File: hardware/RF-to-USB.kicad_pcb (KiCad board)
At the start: 4 copper layers, 48 x 21.5 mm, 6 parts, among them J1 USB_A, J2 Conn_Coaxial, U1 nRF24L01P, U2 STM32L432KBUx, U3 XC6206P332MR, U4 USBLC6-2SC6

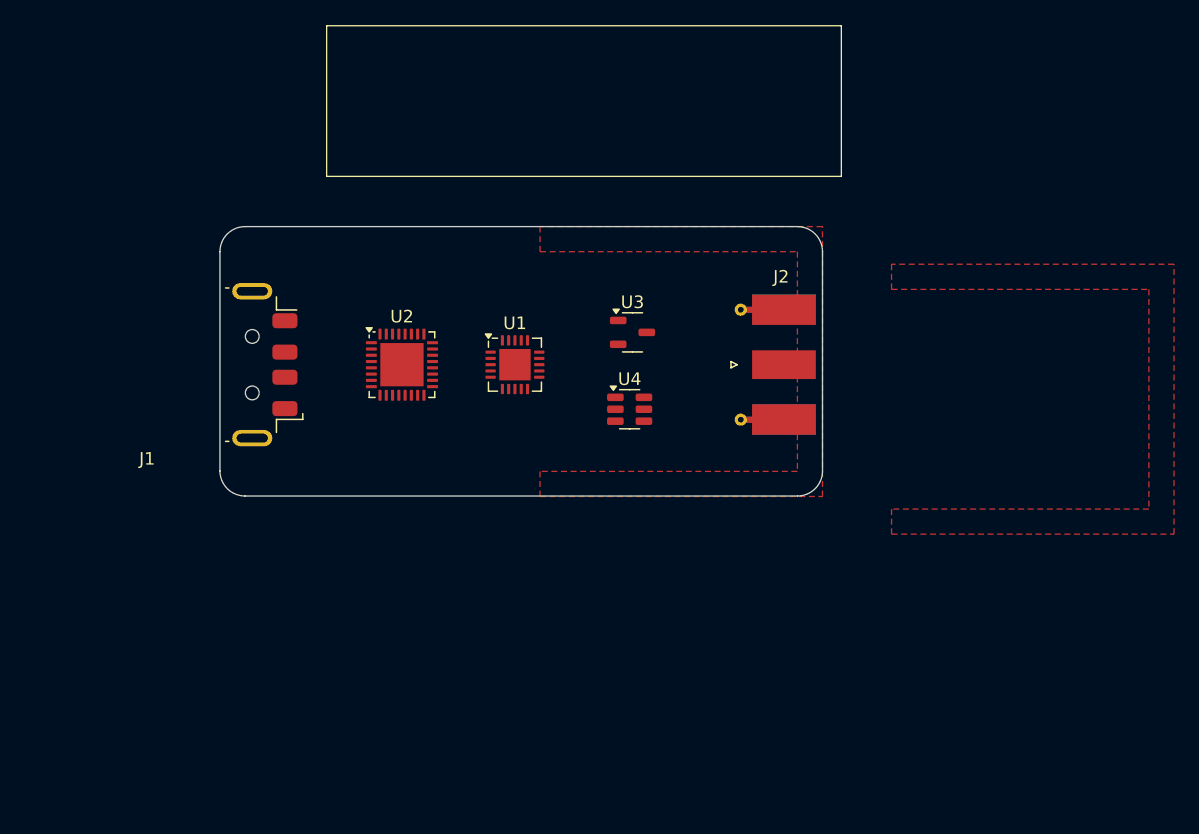
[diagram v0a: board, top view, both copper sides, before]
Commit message: NRF24 transceiver schematic
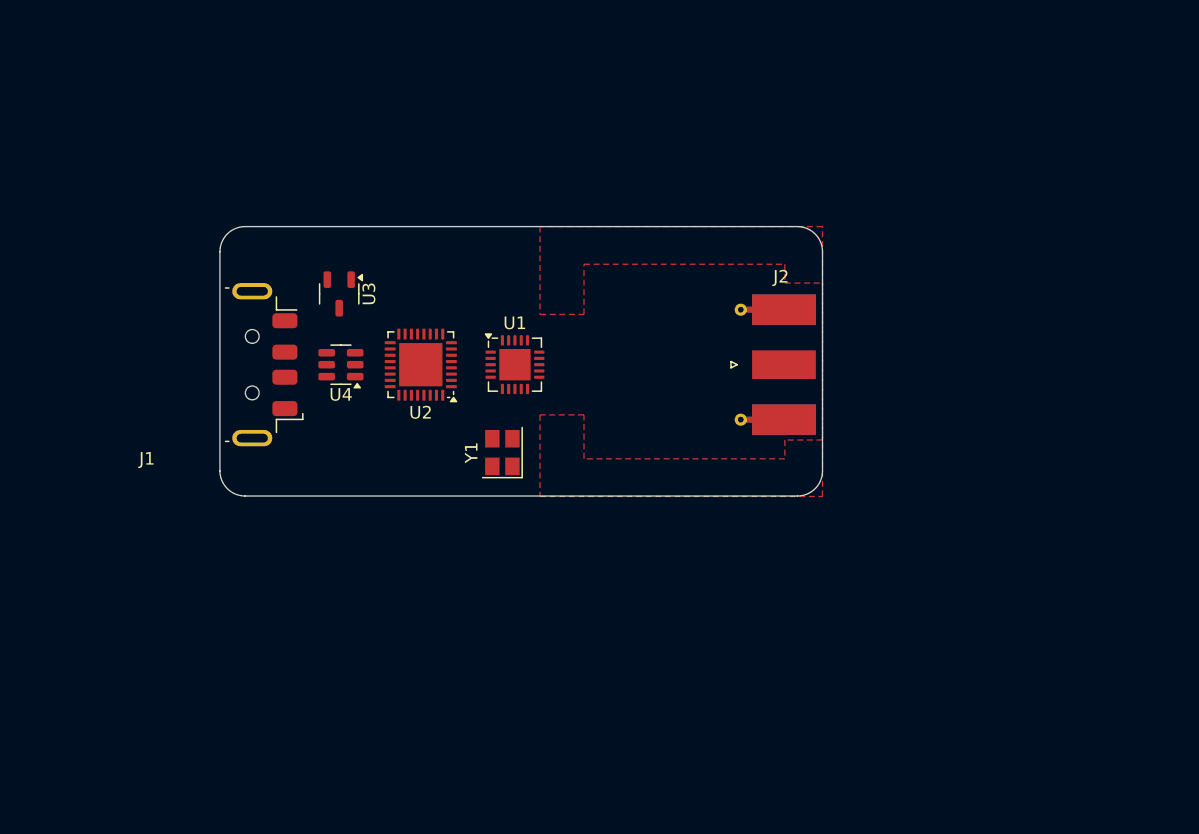
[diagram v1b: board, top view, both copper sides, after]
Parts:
- added Y1: 16MHz, Crystal:Crystal_SMD_SeikoEpson_TSX3225-4Pin_3.2x2.5mm, F.Cu at (98.0, 55.5)
- J2: value Conn_Coaxial -> SMA-F
- moved U3 23.6 mm to (85.0, 42.9), turned to -90 degrees
- moved U4 23.3 mm to (85.1, 48.5), turned to 180 degrees
- moved U2 1.50 mm to (91.5, 48.5), turned to 180 degrees
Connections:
- net Net-(J1-D+) renamed /USB_A_D+
- net Net-(J1-D-) renamed /USB_A_D-
- J2 pad 1: unconnected-(J2-In-Pad1) -> /NRF_ANT
- J2 pad 2: unconnected-(J2-Ext-Pad2) -> GND
- U1 pad 1: unconnected-(U1-CE-Pad1) -> NRF_CE
- U1 pad 10: unconnected-(U1-XC1-Pad10) -> NRF_XC1
- U1 pad 11: unconnected-(U1-VDD_PA-Pad11) -> NRF_VDD_PA
- U1 pad 12: unconnected-(U1-ANT1-Pad12) -> NRF_ANT1
- U1 pad 13: unconnected-(U1-ANT2-Pad13) -> NRF_ANT2
- U1 pad 14: unconnected-(U1-VSS-Pad14) -> GND
- U1 pad 15: unconnected-(U1-VDD-Pad15) -> +3V3
- U1 pad 16: unconnected-(U1-IREF-Pad16) -> Net-(U1-IREF)
- U1 pad 17: unconnected-(U1-VSS-Pad17) -> GND
- U1 pad 18: unconnected-(U1-VDD-Pad18) -> +3V3
- U1 pad 19: unconnected-(U1-DVDD-Pad19) -> Net-(U1-DVDD)
- U1 pad 2: unconnected-(U1-CSN-Pad2) -> SPI3_~{CS}
- U1 pad 20: unconnected-(U1-VSS-Pad20) -> GND
- U1 pad 3: unconnected-(U1-SCK-Pad3) -> SPI3_SCK
- U1 pad 4: unconnected-(U1-MOSI-Pad4) -> SPI3_MOSI
- U1 pad 5: unconnected-(U1-MISO-Pad5) -> SPI3_MISO
- U1 pad 6: unconnected-(U1-IRQ-Pad6) -> NRF_IRQ
- U1 pad 7: unconnected-(U1-VDD-Pad7) -> +3V3
- U1 pad 8: unconnected-(U1-VSS-Pad8) -> GND
- U1 pad 9: unconnected-(U1-XC2-Pad9) -> NRF_XC2
- U2 pad 29: SPI3_CS -> SPI3_~{CS}

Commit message: display footprint
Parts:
- added SW1: BTN1, RF-to-USB:Button_TL3301CF260QG, F.Cu at (128.0, 33.5)
- added SW2: BTN2, RF-to-USB:Button_TL3301CF260QG, F.Cu at (106.5, 30.0)
- added U5: OLED, RF-to-USB:Display_Fermion_OLED_128_32, F.Cu at (103.5, 48.5)
- U1, U2, U3, U4, Y1: moved to B.Cu
- moved Y1 13.1 mm to (102.0, 43.0), turned to 180 degrees
- moved U3 8.12 mm to (93.0, 41.5), turned to 90 degrees
- moved J2 7.00 mm to (125.7, 48.5)
- moved U2 3.50 mm to (95.0, 48.5)
- moved U1 3.00 mm to (102.0, 48.5)
- moved U4 0.64 mm to (84.5, 48.5)
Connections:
- U2 pad 12: unconnected-(U2-PA6-Pad12) -> BTN1_EXTI
- U2 pad 13: unconnected-(U2-PA7-Pad13) -> BTN2_EXTI
- U2 pad 19: unconnected-(U2-PA9-Pad19) -> I2C_SCL
- U2 pad 20: unconnected-(U2-PA10-Pad20) -> I2C_SDA
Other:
- board size 48 x 21.5 mm -> 55 x 25 mm

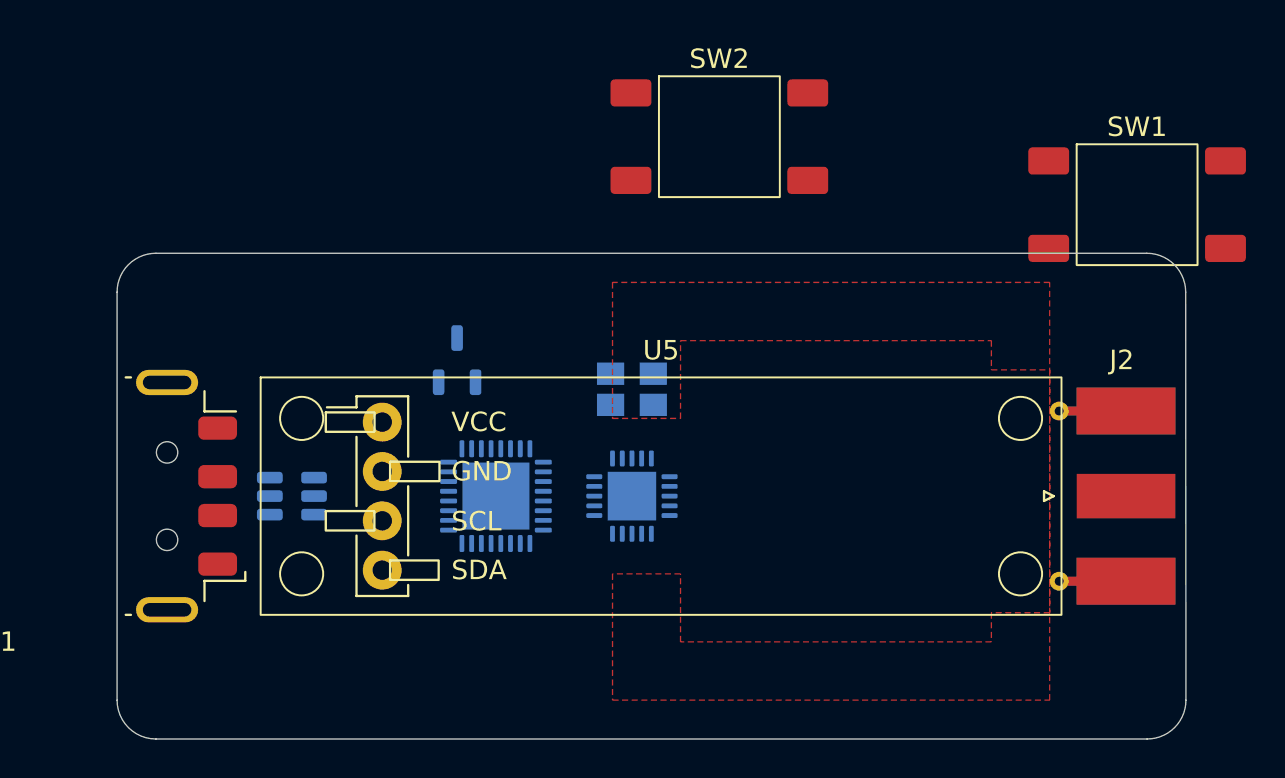
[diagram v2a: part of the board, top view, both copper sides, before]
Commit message: OLED footprint & schematic
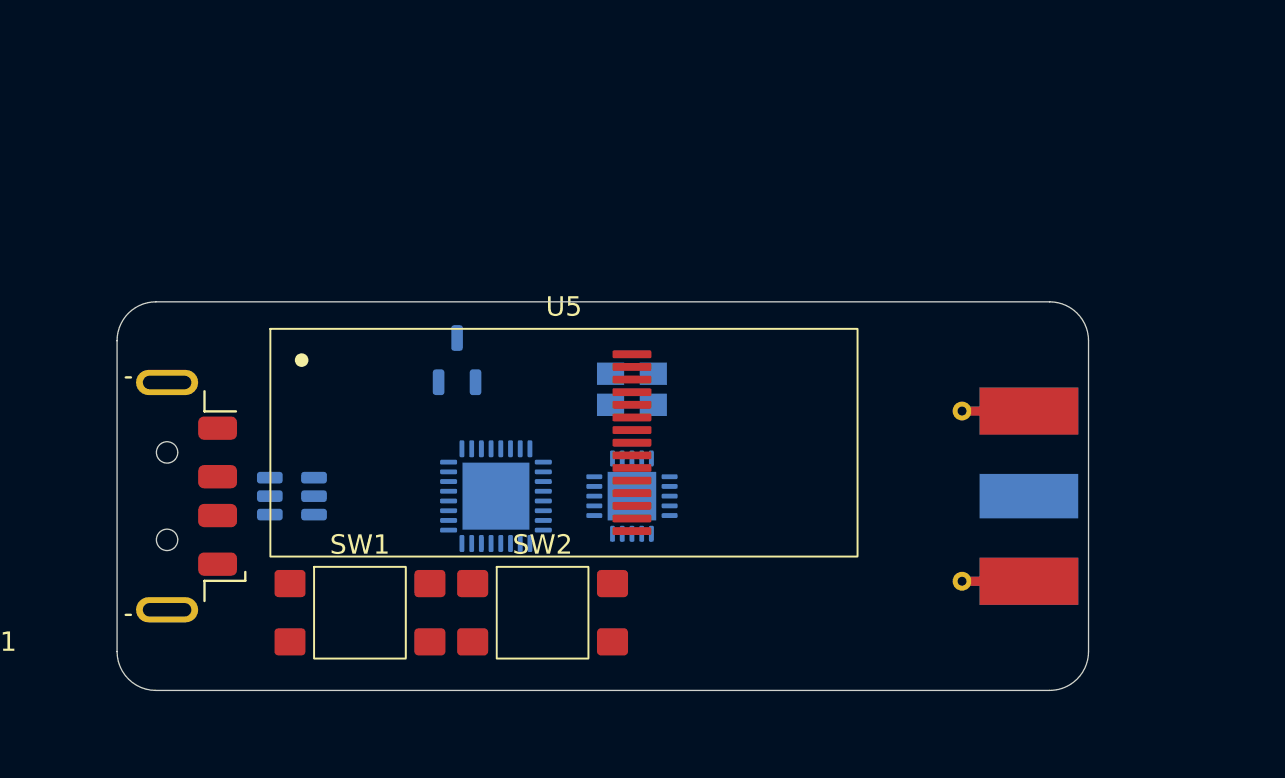
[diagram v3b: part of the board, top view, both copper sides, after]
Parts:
- J2: moved to B.Cu
- SW1, SW2: footprint RF-to-USB:Button_TL3301CF260QG -> RF-to-USB:Button_ESwitch_TL3305
- U5: value OLED -> OLED Display; footprint RF-to-USB:Display_Fermion_OLED_128_32 -> RF-to-USB:Display_Univision_UG-2832HSWEG04
- moved SW1 45.2 mm to (88.0, 54.5)
- moved SW2 26.1 mm to (97.4, 54.5)
- moved U5 5.71 mm to (98.5, 45.8)
- moved J2 5.00 mm to (120.7, 48.5)
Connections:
- SW1 pad 1: unconnected-(SW1-Pad1) -> BTN1_EXTI
- SW1 pad 2: unconnected-(SW1-Pad2) -> BTN1_EXTI
- SW1 pad 3: unconnected-(SW1-Pad3) -> GND
- SW1 pad 4: unconnected-(SW1-Pad4) -> GND
- SW2 pad 1: unconnected-(SW2-Pad1) -> BTN2_EXTI
- SW2 pad 2: unconnected-(SW2-Pad2) -> BTN2_EXTI
- SW2 pad 3: unconnected-(SW2-Pad3) -> GND
- SW2 pad 4: unconnected-(SW2-Pad4) -> GND
- U2 pad 11: unconnected-(U2-PA5-Pad11) -> OLED_DC
- U2 pad 12: BTN1_EXTI -> OLED_CS
- U2 pad 13: BTN2_EXTI -> OLED_RES
- U2 pad 6: unconnected-(U2-PA0-Pad6) -> BTN1_EXTI
- U2 pad 7: unconnected-(U2-PA1-Pad7) -> BTN2_EXTI
- U5 pad 1: +3V3 -> Net-(U5-C2P)
- U5 pad 2: GND -> Net-(U5-C2N)
- U5 pad 3: I2C_SCL -> Net-(U5-C1P)
- U5 pad 4: I2C_SDA -> Net-(U5-C1N)
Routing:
- removed copper zone on F.Cu, net (none)
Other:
- board size 55 x 25 mm -> 50 x 20 mm

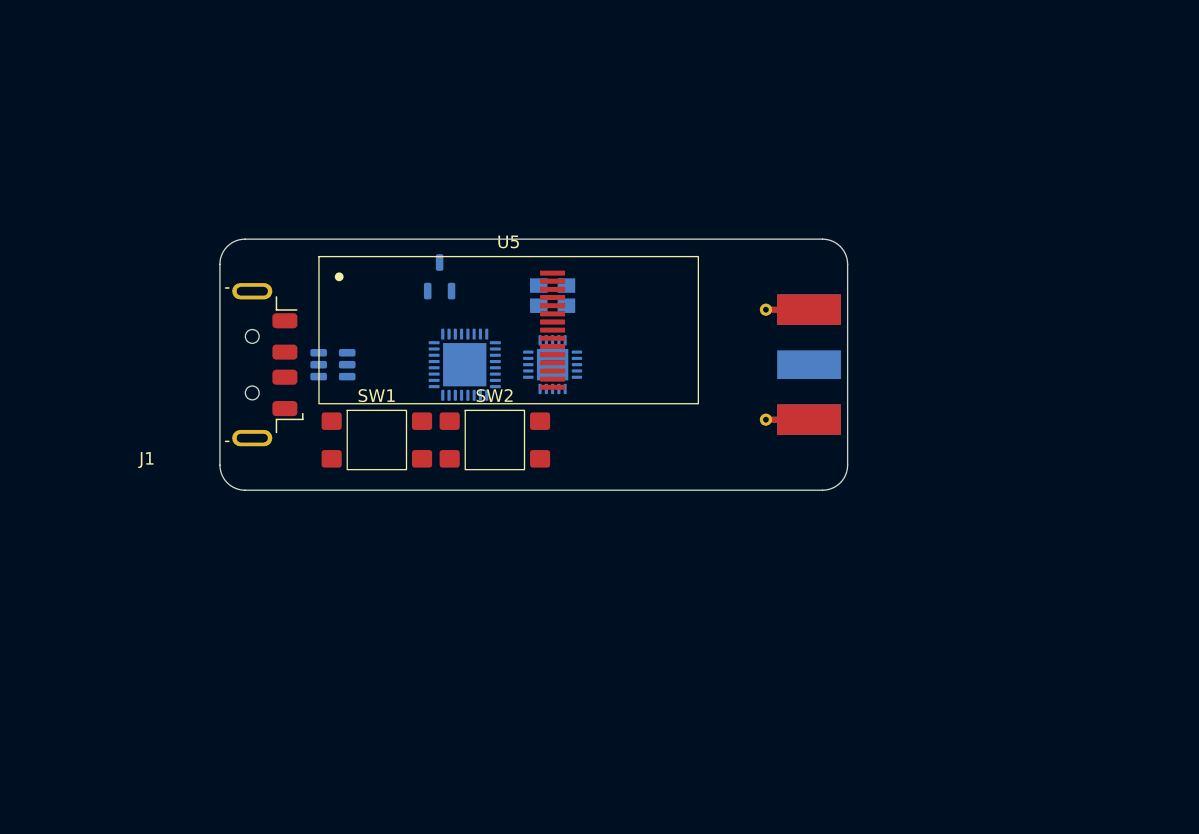
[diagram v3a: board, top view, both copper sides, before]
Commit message: component placement
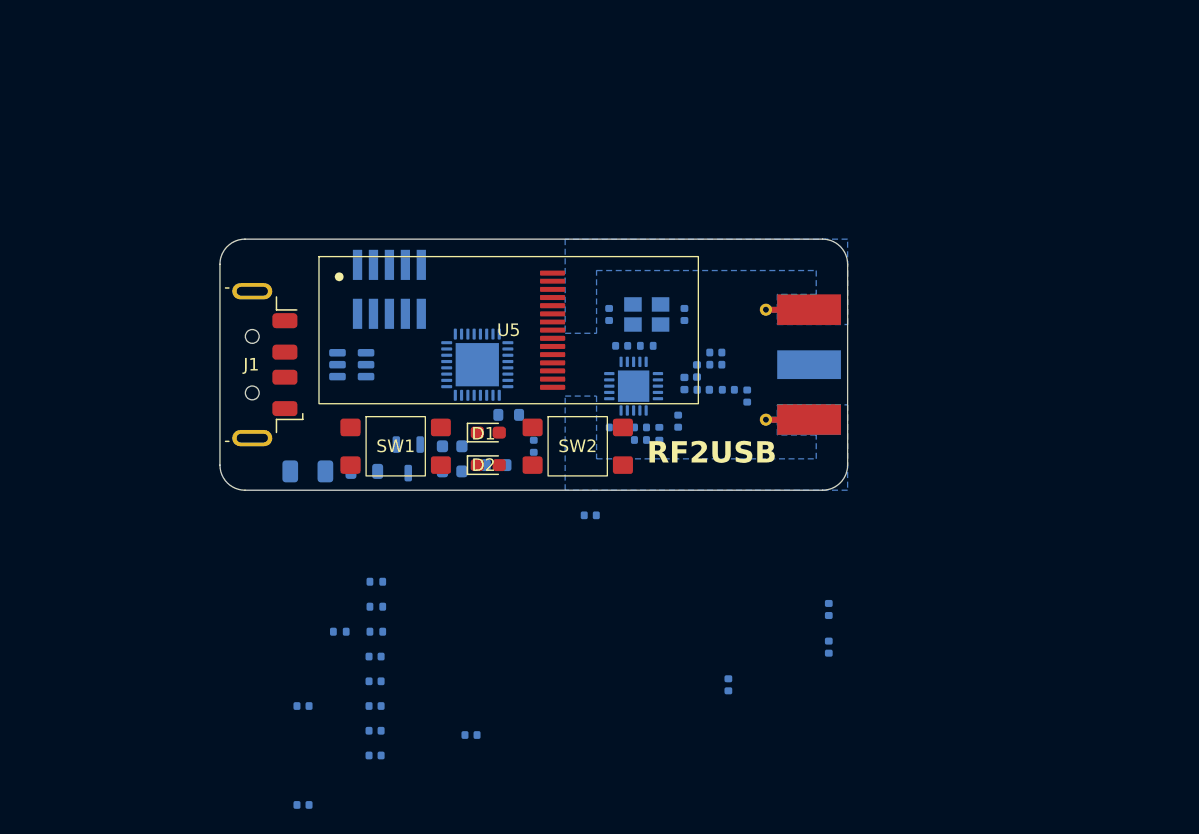
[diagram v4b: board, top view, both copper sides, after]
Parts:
- added C1: 10u, Capacitor_SMD:C_0603_1608Metric, B.Cu at (94.0, 57.0)
- added C10: 10n, Capacitor_SMD:C_0402_1005Metric, B.Cu at (112.0, 53.0)
- added C11: 10n, Capacitor_SMD:C_0402_1005Metric, B.Cu at (107.5, 47.0)
- added C12: 33n, Capacitor_SMD:C_0402_1005Metric, B.Cu at (107.0, 53.5)
- added C13: 1p5, Capacitor_SMD:C_0402_1005Metric, B.Cu at (116.0, 50.5)
- added C14: 1p, Capacitor_SMD:C_0402_1005Metric, B.Cu at (117.5, 51.0)
- added C15: 2n2, Capacitor_SMD:C_0402_1005Metric, B.Cu at (115.0, 48.5)
- added C16: 4p7, Capacitor_SMD:C_0402_1005Metric, B.Cu at (115.0, 47.5)
- added C17: 12p, Capacitor_SMD:C_0402_1005Metric, B.Cu at (112.5, 44.5)
- added C18: 12p, Capacitor_SMD:C_0402_1005Metric, B.Cu at (106.5, 44.5)
- added C19: 1u, Capacitor_SMD:C_0402_1005Metric, B.Cu at (87.9, 79.6)
- added C2: 10u, Capacitor_SMD:C_0603_1608Metric, B.Cu at (94.0, 55.0)
- added C20: 1u, Capacitor_SMD:C_0402_1005Metric, B.Cu at (87.9, 77.7)
- added C21: 2u2, Capacitor_SMD:C_0402_1005Metric, B.Cu at (87.9, 75.7)
- added C22: 2u2, Capacitor_SMD:C_0402_1005Metric, B.Cu at (87.9, 73.7)
- added C23: 1u, Capacitor_SMD:C_0402_1005Metric, B.Cu at (87.9, 71.8)
- added C24: 1u, Capacitor_SMD:C_0402_1005Metric, B.Cu at (95.5, 78.0)
- added C25: 100n, Capacitor_SMD:C_0402_1005Metric, B.Cu at (105.0, 60.5)
- added C26: 100n, Capacitor_SMD:C_0402_1005Metric, B.Cu at (100.5, 55.0)
- added C3: 1u, Capacitor_SMD:C_0402_1005Metric, B.Cu at (82.1, 83.6)
- added C4: 100n, Capacitor_SMD:C_0402_1005Metric, B.Cu at (124.0, 71.0)
- added C5: 100n, Capacitor_SMD:C_0402_1005Metric, B.Cu at (124.0, 68.0)
- added C6: 100n, Capacitor_SMD:C_0402_1005Metric, B.Cu at (116.0, 74.0)
- added C7: 100n, Capacitor_SMD:C_0402_1005Metric, B.Cu at (82.1, 75.7)
- added C8: 10u, Capacitor_SMD:C_0402_1005Metric, B.Cu at (109.0, 54.5)
- added C9: 10n, Capacitor_SMD:C_0402_1005Metric, B.Cu at (109.0, 53.5)
- added D1: GR, LED_SMD:LED_0603_1608Metric_Pad1.05x0.95mm_HandSolder, F.Cu at (96.9, 53.9)
- added D2: YE, LED_SMD:LED_0603_1608Metric_Pad1.05x0.95mm_HandSolder, F.Cu at (96.9, 56.5)
- added F1: 100mA, Fuse:Fuse_1206_3216Metric, B.Cu at (82.5, 57.0)
- added FB1: 100 @ 100MHz, Inductor_SMD:L_0805_2012Metric, B.Cu at (87.0, 57.0)
- added J3: ARM SWD, Connector_PinHeader_1.27mm:PinHeader_2x05_P1.27mm_Vertical_SMD, B.Cu at (89.0, 42.5)
- added L1: 8n2, Inductor_SMD:L_0402_1005Metric, B.Cu at (112.5, 50.0)
- added L2: 2n7, Inductor_SMD:L_0402_1005Metric, B.Cu at (113.5, 49.0)
- added L3: 3n9, Inductor_SMD:L_0402_1005Metric, B.Cu at (114.0, 50.5)
- added R1: 10k, Resistor_SMD:R_0402_1005Metric, B.Cu at (85.0, 69.8)
- added R2: 2k2, Resistor_SMD:R_0603_1608Metric, B.Cu at (98.5, 52.5)
- added R3: 2k2, Resistor_SMD:R_0603_1608Metric, B.Cu at (97.5, 56.5)
- added R4: 22k, Resistor_SMD:R_0402_1005Metric, B.Cu at (110.5, 54.0)
- added R5: 1M, Resistor_SMD:R_0402_1005Metric, B.Cu at (109.5, 47.0)
- added R6: 390k, Resistor_SMD:R_0402_1005Metric, B.Cu at (88.0, 69.8)
- added R7: 4k7, Resistor_SMD:R_0402_1005Metric, B.Cu at (88.0, 67.8)
- added R8: 4k7, Resistor_SMD:R_0402_1005Metric, B.Cu at (88.0, 65.8)
- moved U3 14.7 mm to (90.5, 56.0), turned to -90 degrees
- moved Y1 7.65 mm to (109.5, 44.5)
- moved U1 6.68 mm to (108.5, 50.2)
- moved SW2 6.62 mm to (104.0, 55.0)
- moved SW1 1.58 mm to (89.5, 55.0)
- moved U4 1.50 mm to (86.0, 48.5)
- moved U2 1.00 mm to (96.0, 48.5)
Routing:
- added copper zone on In2.Cu, net +3V3
- added copper zone on B.Cu, net GND
- added copper zone on In1.Cu, net GND
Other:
- board text added: "RF2USB"

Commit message: routing updates
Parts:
- moved C24 54.0 mm to (64.7, 33.6)
- moved C19 51.8 mm to (60.7, 35.5)
- moved C20 51.8 mm to (60.7, 33.5)
- moved C21 51.8 mm to (60.7, 31.6)
- moved C22 45.8 mm to (62.6, 35.5)
- moved C23 45.8 mm to (62.6, 33.6)
- moved R6 45.8 mm to (62.7, 31.6)
- moved C3 45.5 mm to (95.2, 40.0), turned to -90 degrees
- moved C5 39.0 mm to (92.5, 45.0), turned to -135 degrees
- moved C6 37.0 mm to (98.2, 41.5)
- moved C7 33.2 mm to (81.5, 42.5), turned to -90 degrees
- moved C4 30.9 mm to (99.5, 52.2), turned to 45 degrees
- moved R1 24.9 mm to (100.8, 50.5), turned to 90 degrees
- moved C25 20.2 mm to (86.0, 53.8)
- moved R8 16.9 mm to (100.5, 54.5), turned to 180 degrees
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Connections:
- U2 pad 19: I2C_SCL -> unconnected-(U2-PA9-Pad19)
- U2 pad 2: /OSC_IN -> unconnected-(U2-PC14-Pad2)
- U2 pad 20: I2C_SDA -> unconnected-(U2-PA10-Pad20)
- U2 pad 3: /OSC_OUT -> unconnected-(U2-PC15-Pad3)
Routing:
- net GND: track 0.00 -> 76.4 mm, vias 0 -> 32
- net BTN1_EXTI: track 0.00 -> 24.2 mm, vias 0 -> 1
- net +3V3: track 0.00 -> 22.2 mm, vias 0 -> 10
- net BTN2_EXTI: track 0.00 -> 18.1 mm, vias 0 -> 1
- net SWCLK: track 0.00 -> 15.7 mm
- net USB_D-: track 0.00 -> 13.9 mm
- net USB_D+: track 0.00 -> 13.9 mm
- net SPI3_SCK: track 0.00 -> 12.7 mm, vias 0 -> 2
- net SWDIO: track 0.00 -> 11.8 mm
- net /LED_TX: track 0.00 -> 11.7 mm, vias 0 -> 1
- net +5V: track 0.00 -> 11.4 mm, vias 0 -> 7
- net NRF_IRQ: track 0.00 -> 10.7 mm
- net /LED_RX: track 0.00 -> 10.3 mm, vias 0 -> 1
- net SPI3_MISO: track 0.00 -> 9.77 mm, vias 0 -> 1
- net SPI3_~{CS}: track 0.00 -> 8.89 mm
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- added copper zone on B.Cu, net +3V3
- added copper zone on B.Cu, net +5V
- added copper zone on F.Cu, net +5V
- added copper zone on F.Cu, net BTN1_EXTI
- added copper zone on F.Cu, net BTN2_EXTI
- added copper zone on F.Cu, net GND
- added copper zone on B.Cu, net Net-(F1-Pad2)
- added copper zone on B.Cu, net Net-(U3-VI)
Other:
- board text added: "0.3424 mm"
- board text added: "0.3493 mm"
- board text added: "4.4"
- board text added: "Coplanar Single Ended (50 ohm)"
- board text added: "JLC04161H-7628"
- board text added: "Prepreg dielectric constant"
- board text added: "Single Ended (Non Coplanar, 50 ohm)"
- board text added: "more vias to 3v3"
